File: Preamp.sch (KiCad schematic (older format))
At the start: 141 parts, among them J1 Conn_01x03, J10 RCAJack, J11 XLR4BODYPIN, J12 XLR4BODYPIN, J13 XLR4BODYPIN, J2 Conn_01x02, J25 Conn_01x01, J26 Conn_01x01, J27 Conn_01x01, J28 Conn_01x01, J3 Conn_01x02, J4 RCAJack, J5 RCAJack, J6 Conn_01x01, J7 Conn_01x01, J8 Conn_01x01, J9 Conn_01x01, SW1 SW_SPST, U1 LM317, U2 LM337, U3 LM4562, U4 LM4562, U5 LM4562, U6 LM4562, U7 THAT1646, U8 THAT1646, U9 THAT1646

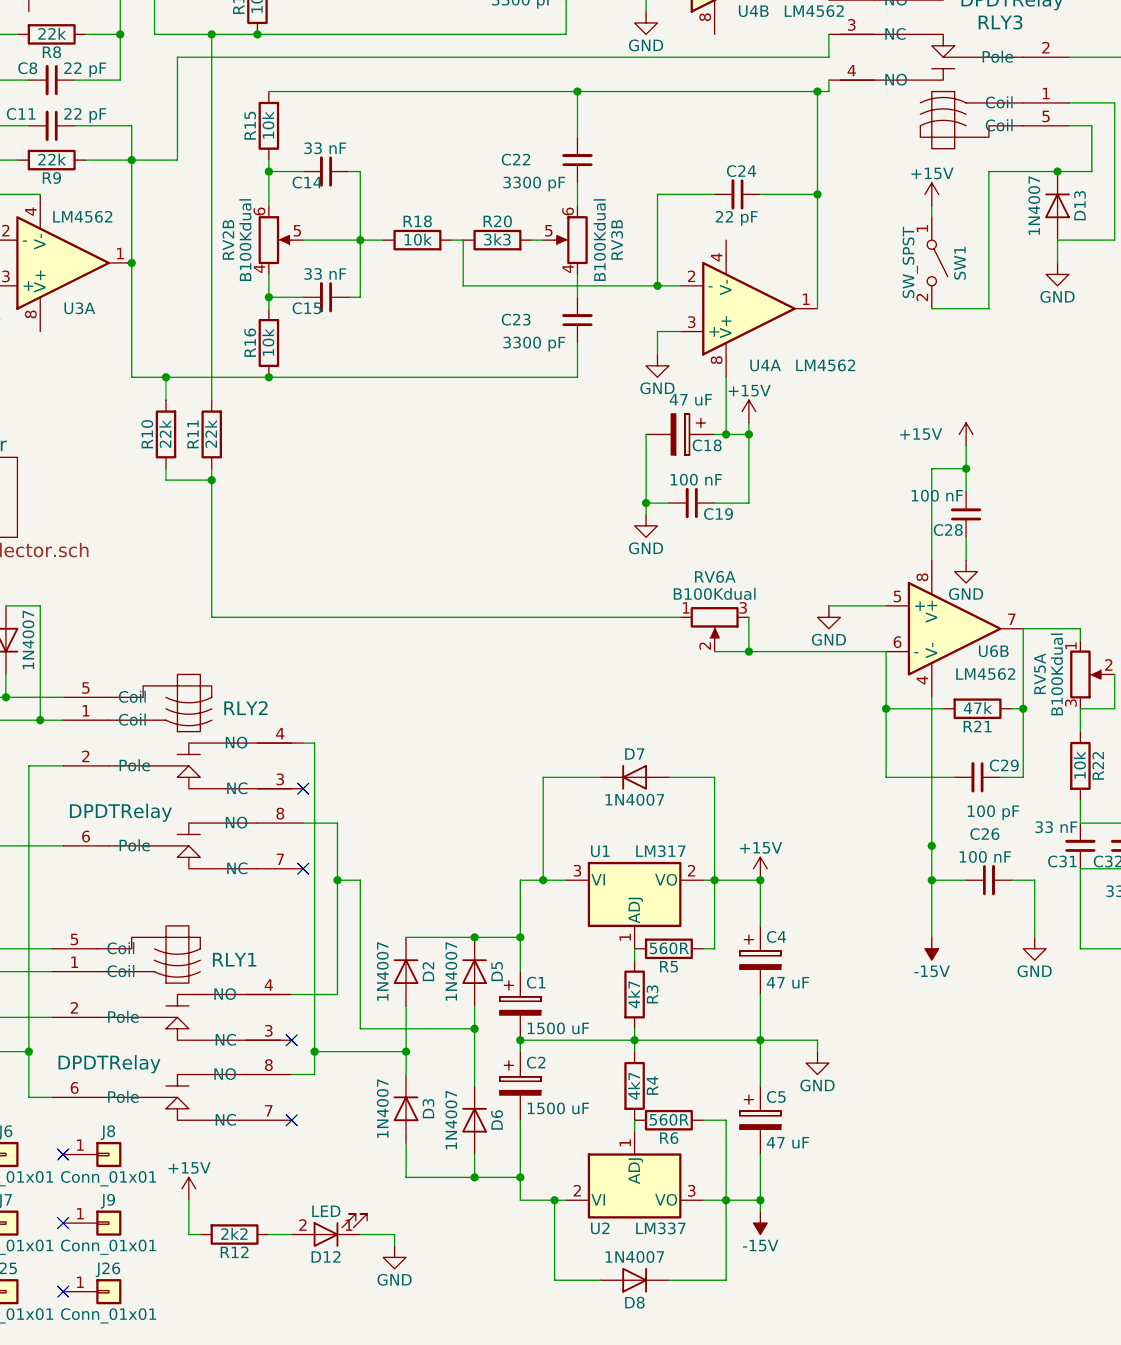
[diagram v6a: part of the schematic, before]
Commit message: remove screwy UVLO
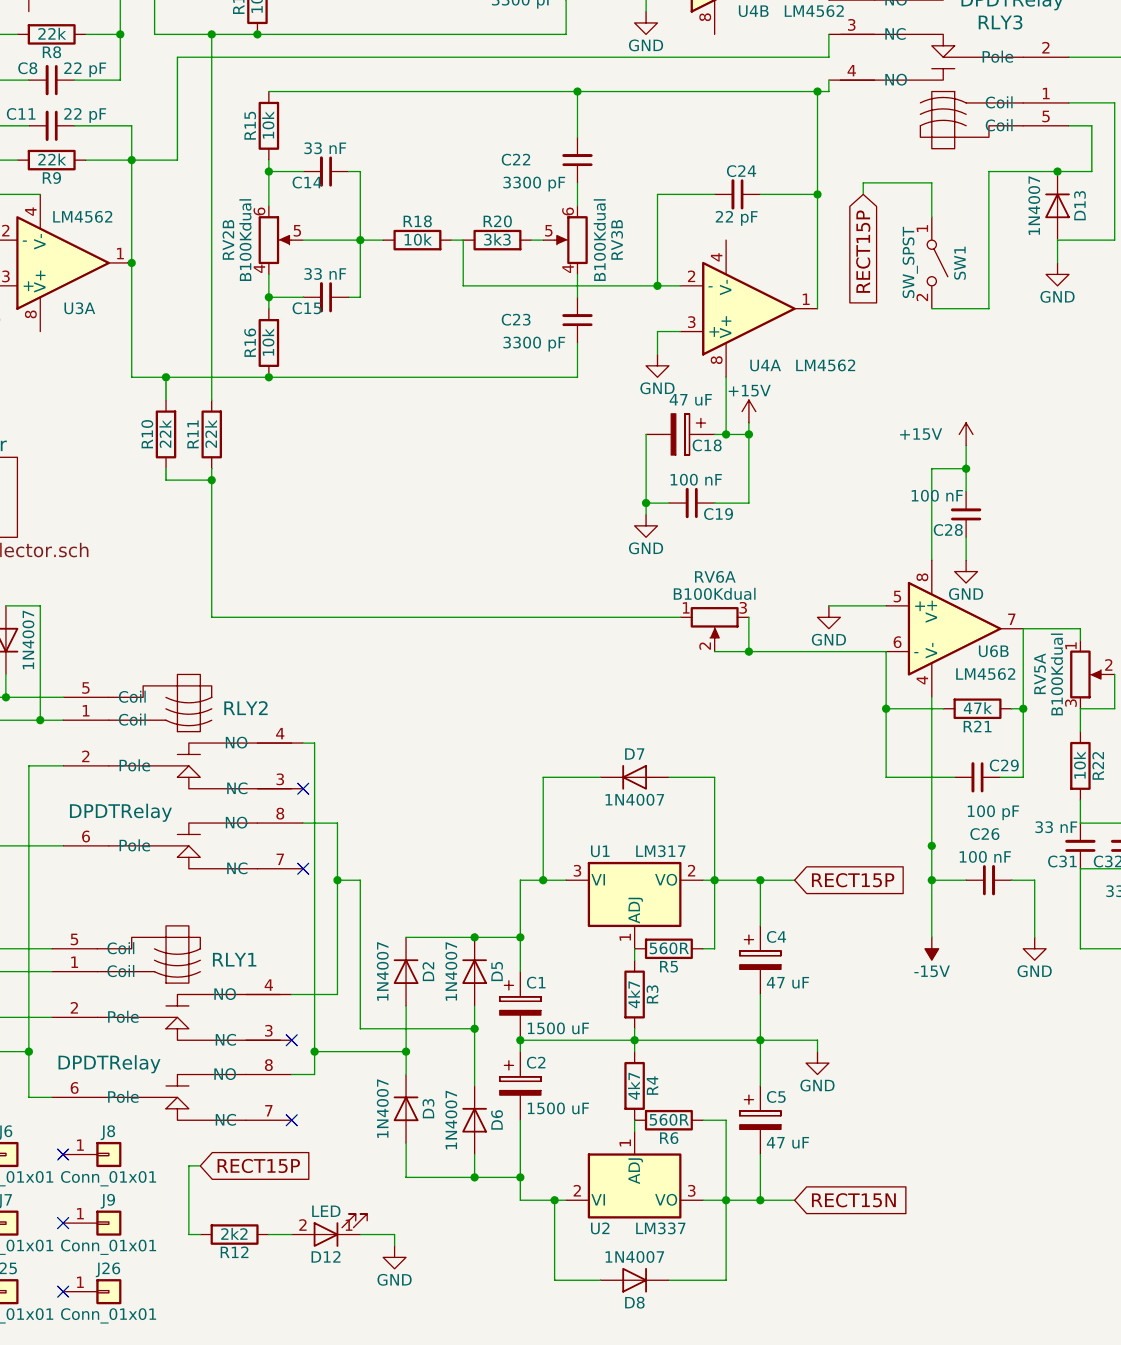
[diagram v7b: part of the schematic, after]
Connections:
- net +15V: no longer C4.1, D7.2 (A), R12.2, R5.1, SW1.1 (A), U1.2 (VO)
- net -15V: no longer C5.2, D8.1 (K), R6.1, U2.3 (VO)
- new net RECT15N: C5.2, D8.1 (K), R6.1, U2.3 (VO)
- new net RECT15P: C4.1, D7.2 (A), R12.2, R5.1, SW1.1 (A), U1.2 (VO)

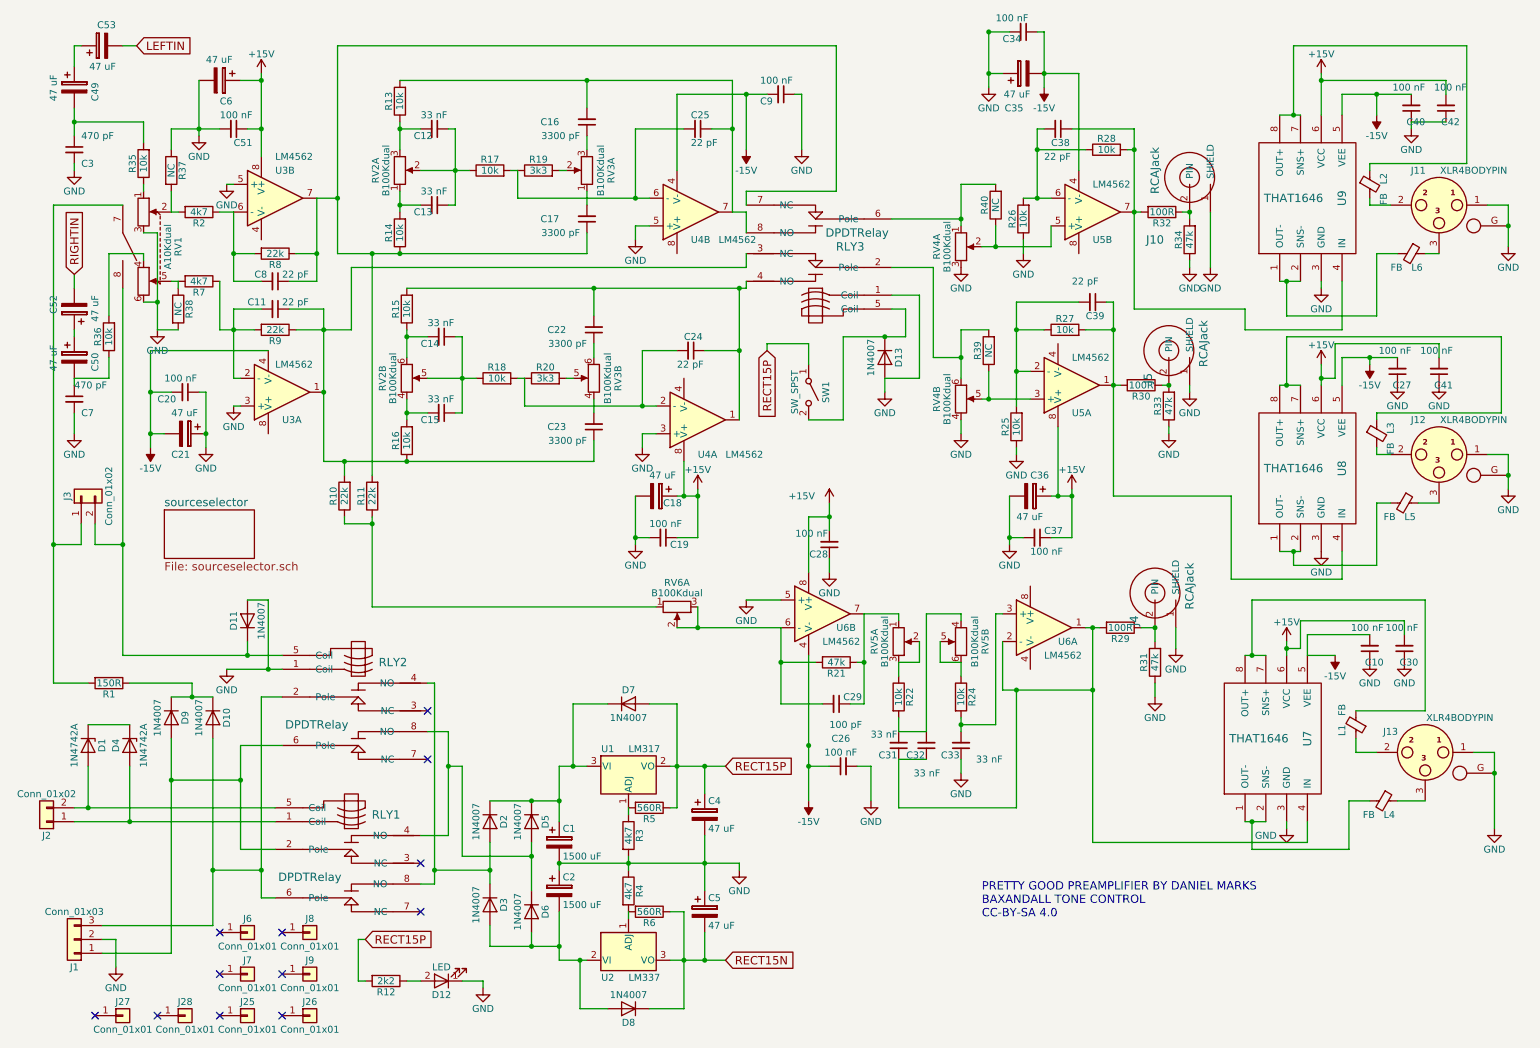
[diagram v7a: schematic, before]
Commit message: Now grounds all of the outputs when supply is below 20 V
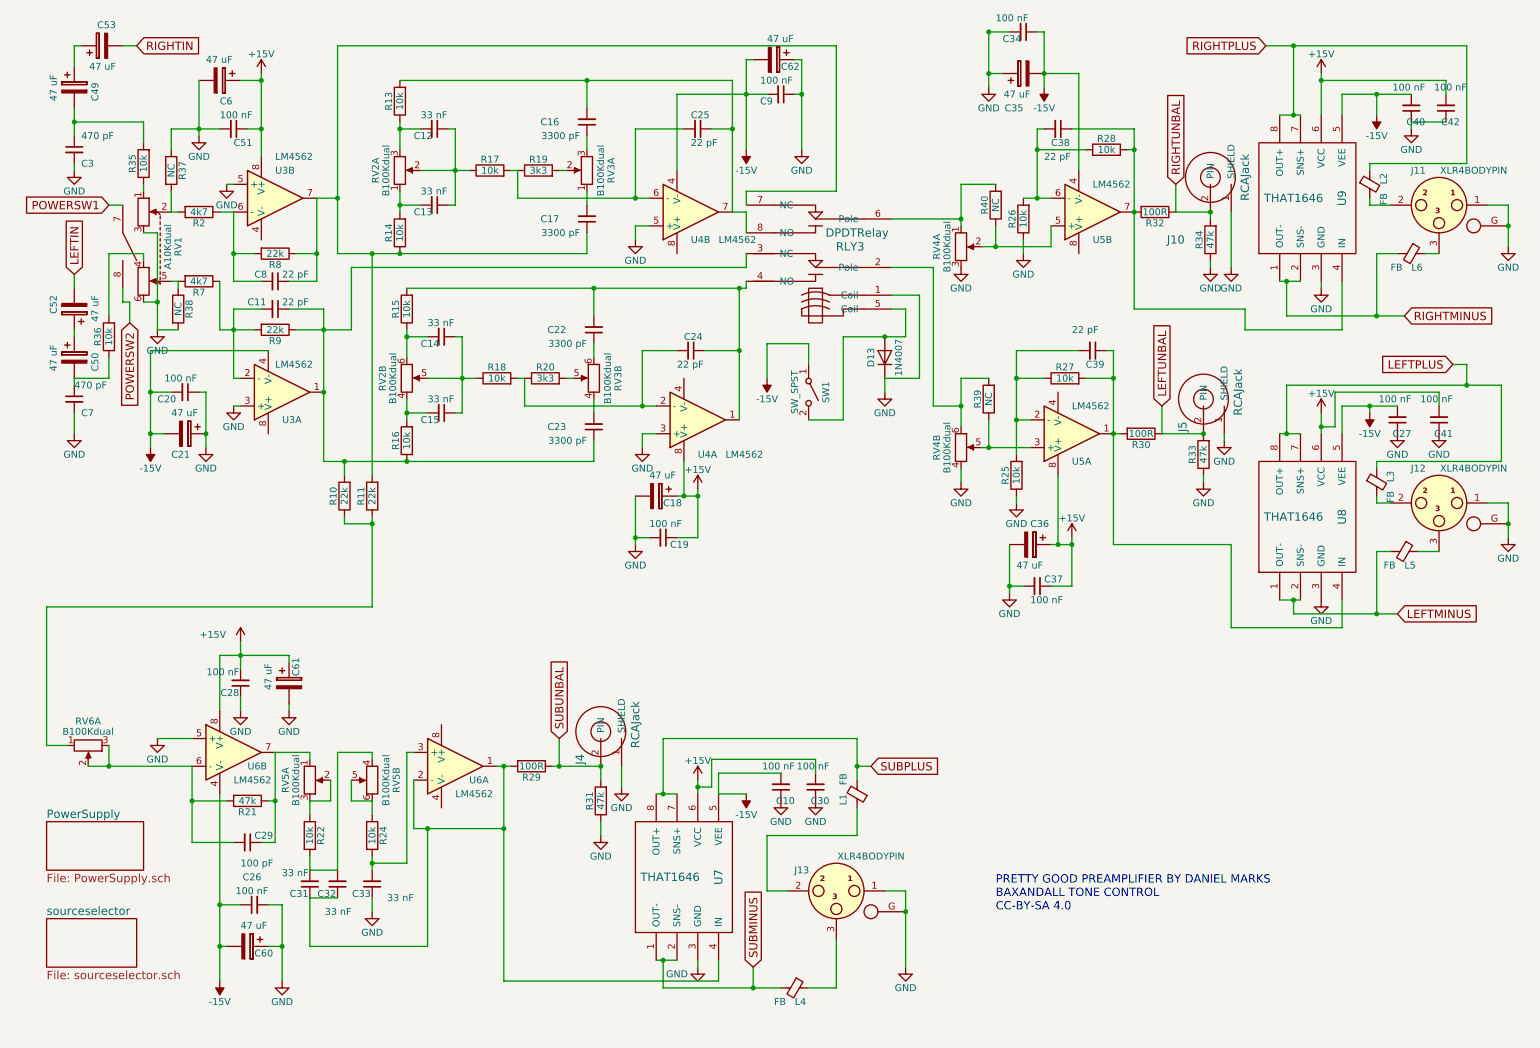
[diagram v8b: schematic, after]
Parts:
- removed C1, C2: 1500 uF, Capacitors_THT:CP_Radial_D10.0mm_P5.00mm, symbol CP
- removed C4, C5: 47 uF, Capacitors_THT:CP_Radial_D7.5mm_P2.50mm, symbol CP
- removed D1, D4: 1N4742A, Diodes_THT:D_DO-41_SOD81_P7.62mm_Horizontal, symbol D_Zener
- removed D10, D11, D2, D3, D5, D6, D7, D8, D9: 1N4007, Diodes_THT:D_DO-41_SOD81_P7.62mm_Horizontal, symbol D
- removed D12: LED, LEDs:LED_D5.0mm, symbol LED
- removed J1: Conn_01x03, Connectors_Terminal_Blocks:TerminalBlock_bornier-3_P5.08mm, symbol Conn_01x03
- removed J2, J3: Conn_01x02, Connectors_Terminal_Blocks:TerminalBlock_bornier-2_P5.08mm, symbol Conn_01x02
- removed J25, J26, J27, J28, J6, J7, J8, J9: Conn_01x01, Connectors:1pin, symbol Conn_01x01
- removed R1: 150R, Resistors_THT:R_Axial_DIN0309_L9.0mm_D3.2mm_P12.70mm_Horizontal, symbol R
- removed R12: 2k2, Resistors_THT:R_Axial_DIN0207_L6.3mm_D2.5mm_P7.62mm_Horizontal, symbol R
- removed R3, R4: 4k7, Resistors_THT:R_Axial_DIN0207_L6.3mm_D2.5mm_P7.62mm_Horizontal, symbol R
- removed R5, R6: 560R, Resistors_THT:R_Axial_DIN0207_L6.3mm_D2.5mm_P7.62mm_Horizontal, symbol R
- removed RLY1, RLY2: DPDTRelay, Preamp:G2VRelay, symbol DPDTRelay
- removed U1: LM317, TO_SOT_Packages_THT:TO-220-3_Vertical, symbol LM317_3PinPackage
- removed U2: LM337, TO_SOT_Packages_THT:TO-220-3_Vertical, symbol LM337_TO220
- added C60, C61, C62: 47 uF, Capacitors_THT:CP_Radial_D5.0mm_P2.50mm, symbol CP
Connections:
- net RECT15P is gone; now on net -15V: SW1.1 (A)
- net +15V: now also C61.1
- net -15V: now also C60.2, C62.2
- net GND: now also D13.1 (K), C60.1, C61.2, C62.1; no longer D13.2 (A)
- net LEFTIN: now also C52.2; no longer C53.2
- net RIGHTIN: now also C53.2; no longer C52.2
- net POWERSW1: now reaches RV1.7 (SW1)
- net POWERSW2: now reaches RV1.8
- net SUBUNBAL: now reaches J4.2 (PIN), R29.1, R31.2
- net RIGHTUNBAL: now reaches J10.2 (PIN), R32.1, R34.2
- net RIGHTMINUS: now reaches L6.2, U9.1 (OUT-), U9.2 (SNS-)
- net RIGHTPLUS: now reaches L2.1, U9.7 (SNS+), U9.8 (OUT+)
- net LEFTMINUS: now reaches L5.2, U8.1 (OUT-), U8.2 (SNS-)
- net LEFTPLUS: now reaches L3.1, U8.7 (SNS+), U8.8 (OUT+)
- net SUBMINUS: now reaches L4.2, U7.1 (OUT-), U7.2 (SNS-)
- net SUBPLUS: now reaches L1.2, U7.7 (SNS+), U7.8 (OUT+)
- net LEFTUNBAL: now reaches J5.2 (PIN), R30.1, R33.2
- net at RLY3.5 (Coil), SW1.2 (B): now also D13.2 (A); no longer D13.1 (K)
- no-connect marks 12 -> 0
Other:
- moved on the sheet: C10, C26, C27, C28, C29, C30, C31, C32, C33, C36, C37, C39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
